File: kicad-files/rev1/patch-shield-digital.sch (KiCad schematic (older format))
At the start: 127 parts

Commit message: split patch-shield into analogue and digital boards
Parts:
- removed P?: CONN_20X2, symbol CONN_20X2
- removed P? (x33): CONN_1, symbol CONN_1
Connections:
- net labels removed: +5VA, AGND, BIASOUT, IN1N, IN1P, IN2N, IN2P, IN3N, IN3P, IN4N, IN4P, IN5N, IN5P, IN6N, IN6P, IN7N, IN7P, IN8N, IN8P
- wire segments 456 -> 375

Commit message: bring ADS129x_GPIO headers up to the digital shield
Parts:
- added P?: CONN_4, symbol CONN_4
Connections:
- net labels added: ADS129x_GPIO1, ADS129x_GPIO2, ADS129x_GPIO3, ADS129x_GPIO4
- wire segments 375 -> 379
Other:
- moved on the sheet: D?, L?, P?, R?

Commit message: improve text label names
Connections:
- net labels added: PA16_A0, PA17_SDA1, PA18_SCL1, PA22_A3, PA23_A2, PA24_A1, PA25_MISO, PA26_MOSI, PA27_SCLK, PA28_SS0, PA29_SS1, PA4_A5, PA6_A4, PA8_RX, PA9_TX, PB25_PWM2, PB27_PWM13, PC21_PWM9, PC22_PWM8, PC23_PWM7, PC24_PWM6, PC25_PWM5, PC26_PWM4, PC28_PWM3, PC29_PWM10, PD7_PWM11, PD8_PWM12
- net labels removed: PA16, PA17, PA18, PA22, PA23, PA24, PA25, PA26, PA27, PA28, PA29, PA4, PA6, PA8, PA9, PB25, PB27, PC21, PC22, PC23, PC24, PC25, PC26, PC28, PC29, PD7, PD8
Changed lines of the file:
@@
 $EndComp
 Text Label 16000 5100 0    60   ~ 0
-PA16
+PA16_A0
 Text Label 16000 5200 0    60   ~ 0
-PA24
+PA24_A1
 Text Label 16000 5300 0    60   ~ 0
-PA23
+PA23_A2
 Text Label 16000 5400 0    60   ~ 0
-PA22
+PA22_A3
 Text Label 16000 5500 0    60   ~ 0
-PA6
+PA6_A4
 Text Label 16000 5600 0    60   ~ 0
-PA4
+PA4_A5
 Text Label 20100 5600 2    60   ~ 0
-PA8
+PA8_RX
 Text Label 20100 5500 2    60   ~ 0
-PA9
+PA9_TX
 Text Label 20100 5400 2    60   ~ 0
-PB25
+PB25_PWM2
 Text Label 20100 5300 2    60   ~ 0
-PC28
+PC28_PWM3
 Text Label 20600 5200 2    60   ~ 0
-PA29
+PA29_SS1
 Text Label 20600 5100 2    60   ~ 0
-PC26
+PC26_PWM4
 Text Label 20100 5100 2    60   ~ 0
-PC25
+PC25_PWM5
 Text Label 20100 5000 2    60   ~ 0
-PC24
+PC24_PWM6
 Text Label 20100 4900 2    60   ~ 0
-PC23
+PC23_PWM7
 Text Label 20100 4700 2    60   ~ 0
-PC22
+PC22_PWM8
 Text Label 20100 4600 2    60   ~ 0
-PC21
+PC21_PWM9
 Text Label 20600 4500 2    60   ~ 0
-PA28
+PA28_SS0
 Text Label 20600 4400 2    60   ~ 0
-PC29
+PC29_PWM10
 Text Label 20100 4400 2    60   ~ 0
-PD7
+PD7_PWM11
 Text Label 20100 4300 2    60   ~ 0
-PD8
+PD8_PWM12
 Text Label 20100 4200 2    60   ~ 0
-PB27
+PB27_PWM13
 $Comp
 L GND #PWR?
@@
 $EndComp
 Text Label 20100 3900 2    60   ~ 0
-PA17
+PA17_SDA1
 Text Label 20100 3800 2    60   ~ 0
-PA18
+PA18_SCL1
 NoConn ~ 20100 4000
 $Comp
@@
 $EndComp
 Text Label 19500 6250 2    60   ~ 0
-PA26
+PA26_MOSI
 Text Label 16500 6150 0    60   ~ 0
-PA25
+PA25_MISO
 Text Label 16500 6250 0    60   ~ 0
-PA27
+PA27_SCLK
 Text Label 16500 6350 0    60   ~ 0
 RESET

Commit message: tidy up the labels and wires on the shields
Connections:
- wire segments 379 -> 449

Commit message: Fixed digital part of patch shield to pass ERC
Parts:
- gave numbers to parts that had none: 94
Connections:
- net labels removed: +5V, ADS129x_GPIO1, ADS129x_GPIO2, ADS129x_GPIO3, ADS129x_GPIO4, PA16_A0, PA17_SDA1, PA18_SCL1, PA22_A3, PA23_A2, PA24_A1, PA25_MISO, PA26_MOSI, PA27_SCLK, PA28_SS0, PA29_SS1, PA4_A5, PA6_A4, PA8_RX, PA9_TX, PB25_PWM2, PB27_PWM13, PC21_PWM9, PC22_PWM8, PC23_PWM7, PC24_PWM6, PC25_PWM5, PC26_PWM4, PC28_PWM3, PC29_PWM10, PD7_PWM11, PD8_PWM12, RESET, V_IN
- wire segments 449 -> 407
- no-connect marks 3 -> 39
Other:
- note added: "GPIO"

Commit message: remove RS-485
 The purpose of the RS-485 was to allow us to synch multiple
devices. However, a better way to do this is to inject a counter
into the samples using the USB Start Of Frame which will be
shared by all devices on the same USB bus.
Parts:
- removed C1, C2, C3, C5: 100nF, symbol C
- removed C4: 10uF, symbol C
- removed D17, D35, D36, D37: DOUBLE_SCHOTTKY, symbol DOUBLE_SCHOTTKY
- removed J1, J2: RJ45, symbol RJ45
- removed L1: INDUCTOR, symbol INDUCTOR
- removed P3: CONN_8X2, symbol CONN_8X2
- removed R19: 120, symbol R
- removed R20, R21: 680, symbol R
- removed R22, R24, R25, R26, R28, R9: 1k, symbol R
- removed R23, R27, R29: 100k, symbol R
- removed U1: RS485, symbol RS485
- removed U2: 74HC00, symbol 7400
- removed U3, U4: TS5A4624, symbol TS5A4624
- added P3: CONN_4X2, symbol CONN_4X2
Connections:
- net labels removed: 5V_IN, DAISY_DETECT_NEXT, DAISY_DETECT_NEXT_FILT, DAISY_DETECT_PREVIOUS, DAISY_DETECT_PREVIOUS_FILT, DAISY_ENUMERATION_IN, DAISY_ENUMERATION_IN_FILT, DAISY_ENUMERATION_OUT, DAISY_ENUMERATION_OUT_FILT, RS485_A, RS485_B, RTS2_RS485_DE, RXD2_RS485_R, TXD2_RS485_D
- wire segments 407 -> 226
- no-connect marks 39 -> 37
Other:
- note removed: "Biasing and termination for RS-485"
- note removed: "DAISY CHAIN NEXT"
- note removed: "DAISY CHAIN PREVIOUS"
- note removed: "TODO: Replace with SN74LVC1G00DCKR"
- note removed: "TODO: according to the SN65HVD78D datasheet, \n we may not need the biasing resistors \n (allowing us to eleminate a switch). \n We should discuss this."
- note removed: "e.g. SN65HVD78D"

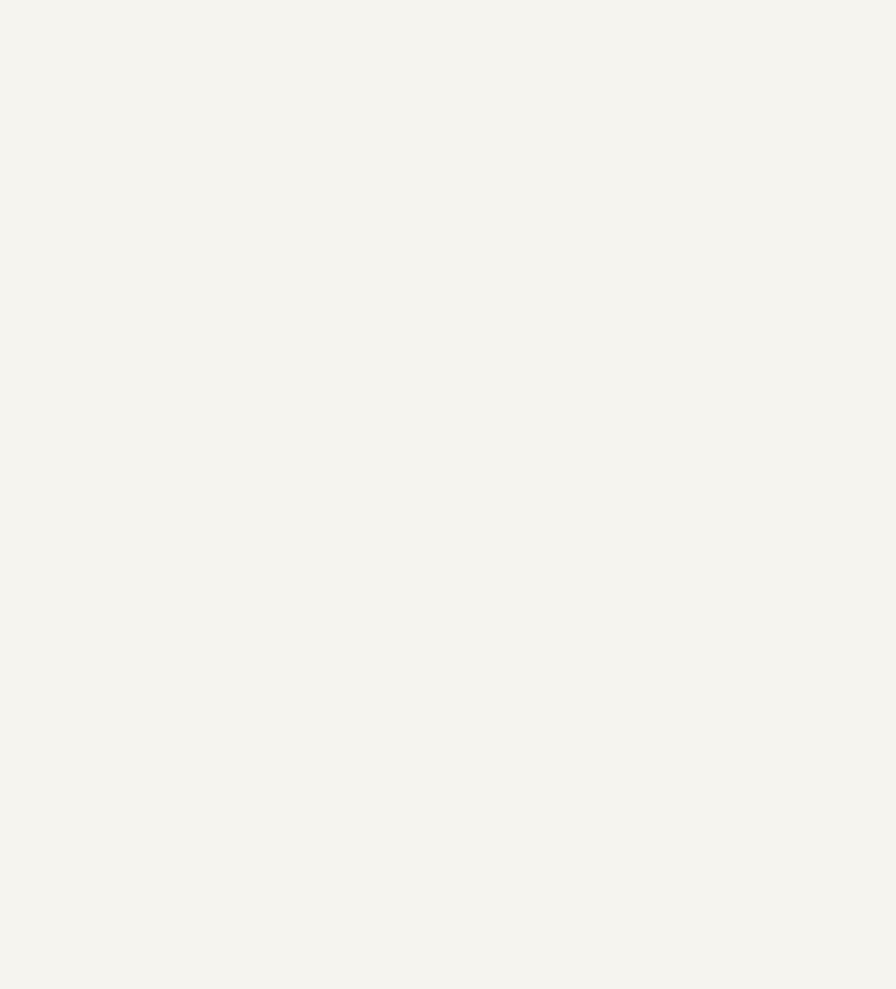
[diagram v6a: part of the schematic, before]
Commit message: added I2C EEPROM to shields
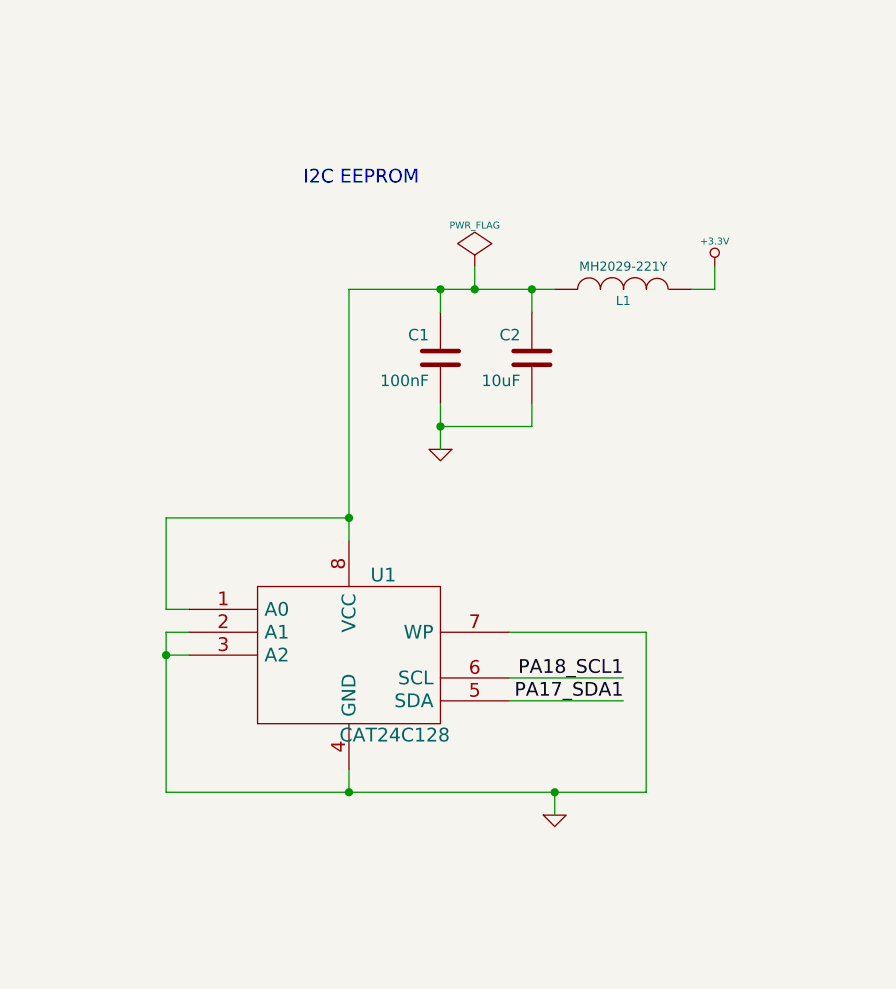
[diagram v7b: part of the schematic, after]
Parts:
- added C1: 100nF, symbol C
- added C2: 10uF, symbol C
- added L1: MH2029-221Y, symbol INDUCTOR
- added U1: CAT24C128, symbol 24C16
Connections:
- net labels added: PA17_SDA1, PA18_SCL1
- wire segments 226 -> 249
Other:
- note added: "I2C EEPROM"
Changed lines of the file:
@@
-EESchema Schematic File Version 2  date Sat 22 Jun 2013 01:17:50 PM CEST
+EESchema Schematic File Version 2  date Sat 22 Jun 2013 01:59:59 PM CEST
 LIBS:power
 LIBS:device
@@
 Comment4 ""
 $EndDescr
+Connection ~ 17500 10800
+Wire Wire Line
+	17500 10800 16700 10800
+Wire Wire Line
+	16700 10800 16700 11200
+Wire Wire Line
+	16700 12000 16700 11300
+Connection ~ 18400 12000
+Wire Wire Line
+	18400 12100 18400 12000
+Wire Wire Line
+	16700 12000 18800 12000
+Wire Wire Line
+	18800 12000 18800 11300
+Wire Wire Line
+	18800 11300 18200 11300
+Wire Wire Line
+	18200 11600 18700 11600
+Wire Wire Line
+	16700 11300 16800 11300
+Wire Wire Line
+	18400 9800 17500 9800
+Wire Wire Line
+	17900 10500 17900 10300
+Connection ~ 17900 9800
+Wire Wire Line
+	17900 9900 17900 9800
+Wire Wire Line
+	18300 9800 18300 9900
+Connection ~ 18300 9800
+Wire Wire Line
+	18050 9800 18050 9700
+Connection ~ 18050 9800
+Wire Wire Line
+	17900 10400 18300 10400
+Wire Wire Line
+	18300 10400 18300 10300
+Connection ~ 17900 10400
+Wire Wire Line
+	19000 9800 19100 9800
+Wire Wire Line
+	19100 9800 19100 9700
+Wire Wire Line
+	16700 11200 16800 11200
+Connection ~ 17500 12000
+Wire Wire Line
+	16800 11400 16700 11400
+Connection ~ 16700 11400
+Wire Wire Line
+	18700 11500 18200 11500
+Wire Wire Line
+	17500 11900 17500 12000
+Wire Wire Line
+	17500 9800 17500 10900
+$Comp
+L 24C16 U1
+U 1 1 51C591AB
+P 17500 11400
+F 0 "U1" H 17650 11750 60  0000 C CNN
+F 1 "CAT24C128" H 17700 11050 60  0000 C CNN
+	1    17500 11400
+	1    0    0    -1
+$EndComp
+$Comp
+L PWR_FLAG #FLG2
+U 1 1 51C591AA
+P 18050 9700
+F 0 "#FLG2" H 18050 9795 30  0001 C CNN
+F 1 "PWR_FLAG" H 18050 9880 30  0000 C CNN
+	1    18050 9700
+	-1   0    0    -1
+$EndComp
+$Comp
+L C C2
+U 1 1 51C591A9
+P 18300 10100
+F 0 "C2" H 18350 10200 50  0000 L CNN
+F 1 "10uF" H 18350 10000 50  0000 L CNN
+	1    18300 10100
+	-1   0    0    -1
+$EndComp
+$Comp
+L INDUCTOR L1
+U 1 1 51C591A8
+P 18700 9800
+F 0 "L1" V 18650 9800 40  0000 C CNN
+F 1 "MH2029-221Y" V 18800 9800 40  0000 C CNN
+	1    18700 9800
+	0    1    -1   0
+$EndComp
+$Comp
+L C C1
+U 1 1 51C591A7
+P 17900 10100
+F 0 "C1" H 17950 10200 50  0000 L CNN
+F 1 "100nF" H 17950 10000 50  0000 L CNN
+	1    17900 10100
+	-1   0    0    -1
+$EndComp
+$Comp
+L +3.3V #PWR27
+U 1 1 51C591A6
+P 19100 9700
+F 0 "#PWR27" H 19100 9660 30  0001 C CNN
+F 1 "+3.3V" H 19100 9810 30  0000 C CNN
+	1    19100 9700
+	-1   0    0    -1
+$EndComp
+$Comp
+L GND #PWR23
+U 1 1 51C591A5
+P 17900 10500
+F 0 "#PWR23" H 17900 10500 30  0001 C CNN
+F 1 "GND" H 17900 10430 30  0001 C CNN
+	1    17900 10500
+	-1   0    0    -1
+$EndComp
+$Comp
+L GND #PWR24
+U 1 1 51C591A4
+P 18400 12100
+F 0 "#PWR24" H 18400 12100 30  0001 C CNN
+F 1 "GND" H 18400 12030 30  0001 C CNN
+	1    18400 12100
+	1    0    0    -1
+$EndComp
+Text Label 18700 11500 2    60   ~ 0
+PA18_SCL1
+Text Label 18700 11600 2    60   ~ 0
+PA17_SDA1
+Text Notes 17300 9350 0    60   ~ 0
+I2C EEPROM
 Connection ~ 18450 8100
 Wire Wire Line
@@
 NoConn ~ 19300 3800
 $Comp
-L GND #PWR25
+L GND #PWR28
 U 1 1 51C4F610
 P 19500 4200
-F 0 "#PWR25" H 19500 4200 30  0001 C CNN
+F 0 "#PWR28" H 19500 4200 30  0001 C CNN
 F 1 "GND" H 19500 4130 30  0001 C CNN
 	1    19500 4200
@@
 $EndComp
 $Comp
-L GND #PWR24
+L GND #PWR26
 U 1 1 51B34D95
 P 19100 6450
-F 0 "#PWR24" H 19100 6450 30  0001 C CNN
+F 0 "#PWR26" H 19100 6450 30  0001 C CNN
 F 1 "GND" H 19100 6380 30  0001 C CNN
 	1    19100 6450
@@
 $EndComp
 $Comp
-L PWR_FLAG #FLG2
+L PWR_FLAG #FLG3
 U 1 1 51B34A47
 P 18650 8000
-F 0 "#FLG2" H 18650 8095 30  0001 C CNN
+F 0 "#FLG3" H 18650 8095 30  0001 C CNN
 F 1 "PWR_FLAG" H 18650 8180 30  0000 C CNN
 	1    18650 8000
@@
 LED_SHIFT_REG_CLEAR
 $Comp
-L GND #PWR23
+L GND #PWR25
 U 1 1 51B34A09
 P 18450 8200
-F 0 "#PWR23" H 18450 8200 30  0001 C CNN
+F 0 "#PWR25" H 18450 8200 30  0001 C CNN
 F 1 "GND" H 18450 8130 30  0001 C CNN
 	1    18450 8200

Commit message: merge GPIO and Supplemental IO connectors
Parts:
- removed L2: INDUCTOR, symbol INDUCTOR
- removed P1: CONN_4, symbol CONN_4
- removed P3: CONN_4X2, symbol CONN_4X2
- added P1: CONN_5X2, symbol CONN_5X2
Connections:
- net labels added: ADS129x_GPIO1, ADS129x_GPIO2, ADS129x_GPIO3, ADS129x_GPIO4
- wire segments 249 -> 250
- no-connect marks 37 -> 32
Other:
- note added: "Supplemental digital IO header"
- note removed: "GPIO"
